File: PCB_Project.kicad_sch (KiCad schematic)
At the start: 0 parts

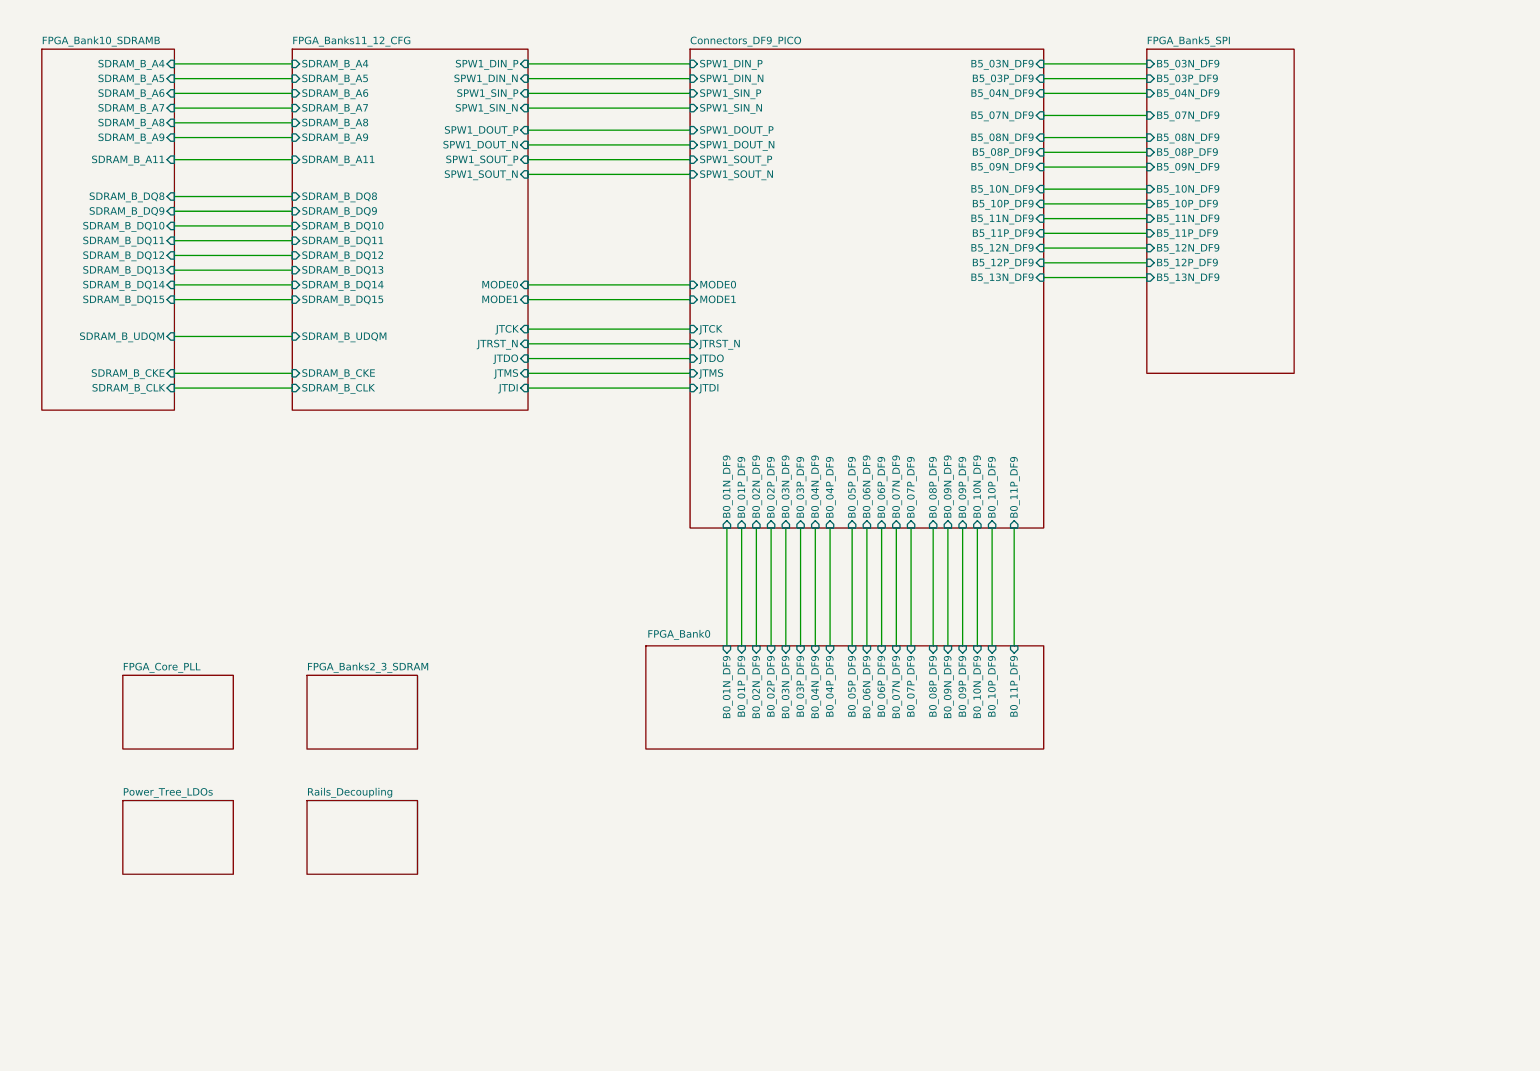
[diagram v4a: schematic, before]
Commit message: pre order checks
ADDED jumper for VDDSENSE remote sensing / 1V2 core PWR for MAX LDO feedback
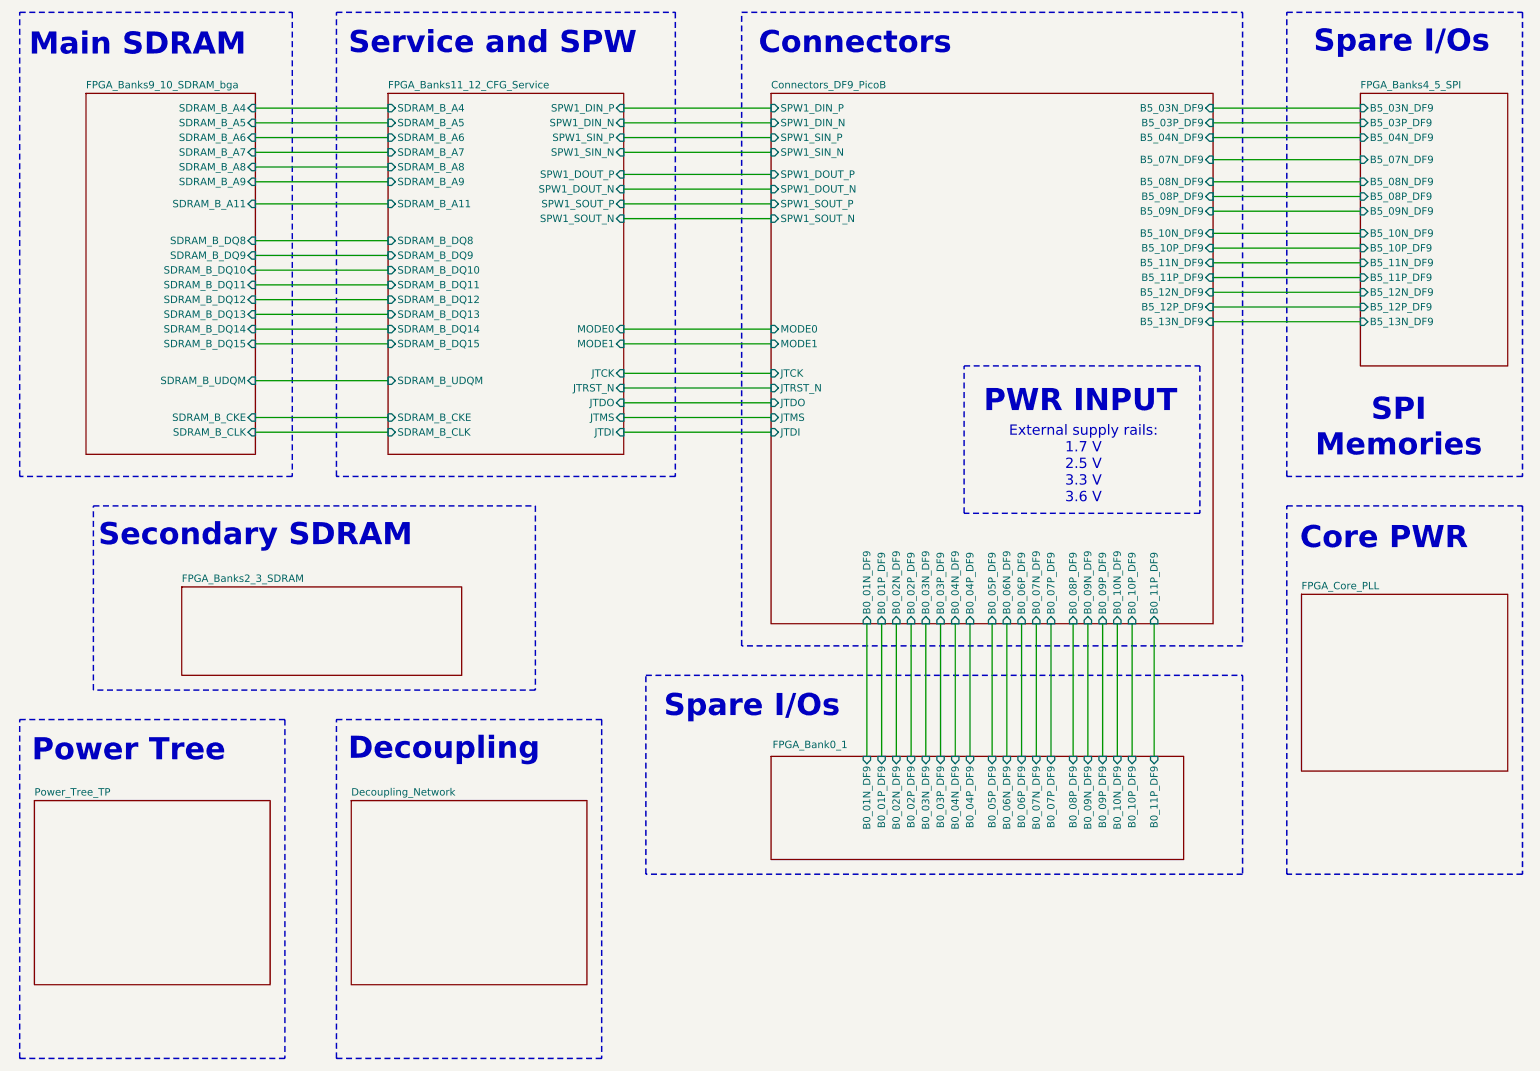
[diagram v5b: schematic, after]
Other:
- sheet Connectors_DF9_PICO renamed Connectors_DF9_PicoB
- sheet FPGA_Bank0 renamed FPGA_Bank0_1
- sheet FPGA_Bank10_SDRAMB renamed FPGA_Banks9_10_SDRAM_bga
- sheet FPGA_Bank5_SPI renamed FPGA_Banks4_5_SPI
- sheet FPGA_Banks11_12_CFG renamed FPGA_Banks11_12_CFG_Service
- sheet Power_Tree_LDOs renamed Power_Tree_TP
- sheet Rails_Decoupling renamed Decoupling_Network
- sheet Connectors_DF9_PicoB: file DF9_CFG_SPW1.kicad_sch -> Connectors_DF9_PicoB.kicad_sch
- sheet Decoupling_Network: file Power_rails.kicad_sch -> Decoupling_Network.kicad_sch
- sheet FPGA_Bank0_1: file debug_uart.kicad_sch -> FPGA_Bank0_1.kicad_sch
- sheet FPGA_Banks11_12_CFG_Service: file config_reset.kicad_sch -> FPGA_Banks11_12_CFG_Service.kicad_sch
- sheet FPGA_Banks2_3_SDRAM: file banks23_SDRAM.kicad_sch -> FPGA_Banks2_3_SDRAM.kicad_sch
- sheet FPGA_Banks4_5_SPI: file bank5_SPI.kicad_sch -> FPGA_Banks4_5_SPI.kicad_sch
- sheet FPGA_Banks9_10_SDRAM_bga: file IO_Connectors_DF9.kicad_sch -> FPGA_Banks9_10_SDRAM_bga.kicad_sch
- sheet FPGA_Core_PLL: file core_cfg.kicad_sch -> FPGA_Core_PLL.kicad_sch
- sheet Power_Tree_TP: file unused.kicad_sch -> Power_Tree_TP.kicad_sch
- note added: "Connectors"
- note added: "Core PWR"
- note added: "Decoupling"
- note added: "External supply rails: 1.7 V 2.5 V 3.3 V 3.6 V"
- note added: "Main SDRAM"
- note added: "PWR INPUT"
- note added: "Power Tree"
- note added: "SPI Memories"
- note added: "Secondary SDRAM"
- note added: "Service and SPW"
- note added: "Spare I/Os"
- company: (none) -> KTH Royal Institute of Technology
- title: (none) -> DataHub+ Top-Level Schematic
